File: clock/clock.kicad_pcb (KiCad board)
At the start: 2 copper layers, 100 x 50 mm, 51 parts, among them J1 Conn_01x16_Male, J2 Conn_01x16_Male, J3 5v, J4 Conn_01x01_Male, J5 24v, J6 Conn_01x01_Male, U1 iv12, U2 iv12, U3 iv12, U4 iv12, U5 ULN2003, U6 ULN2003, U7 ULN2003, U8 ULN2003

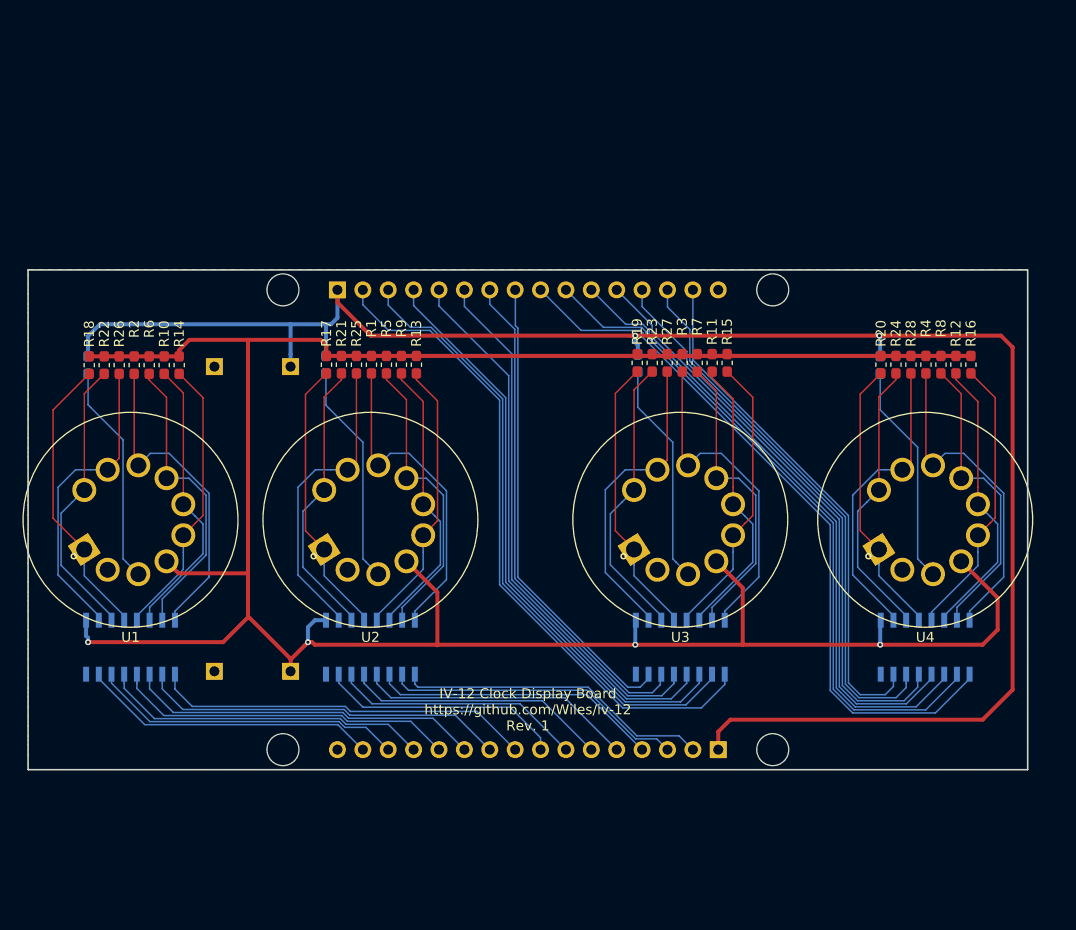
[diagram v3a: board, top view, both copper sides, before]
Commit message: Clock rev 2 with controller
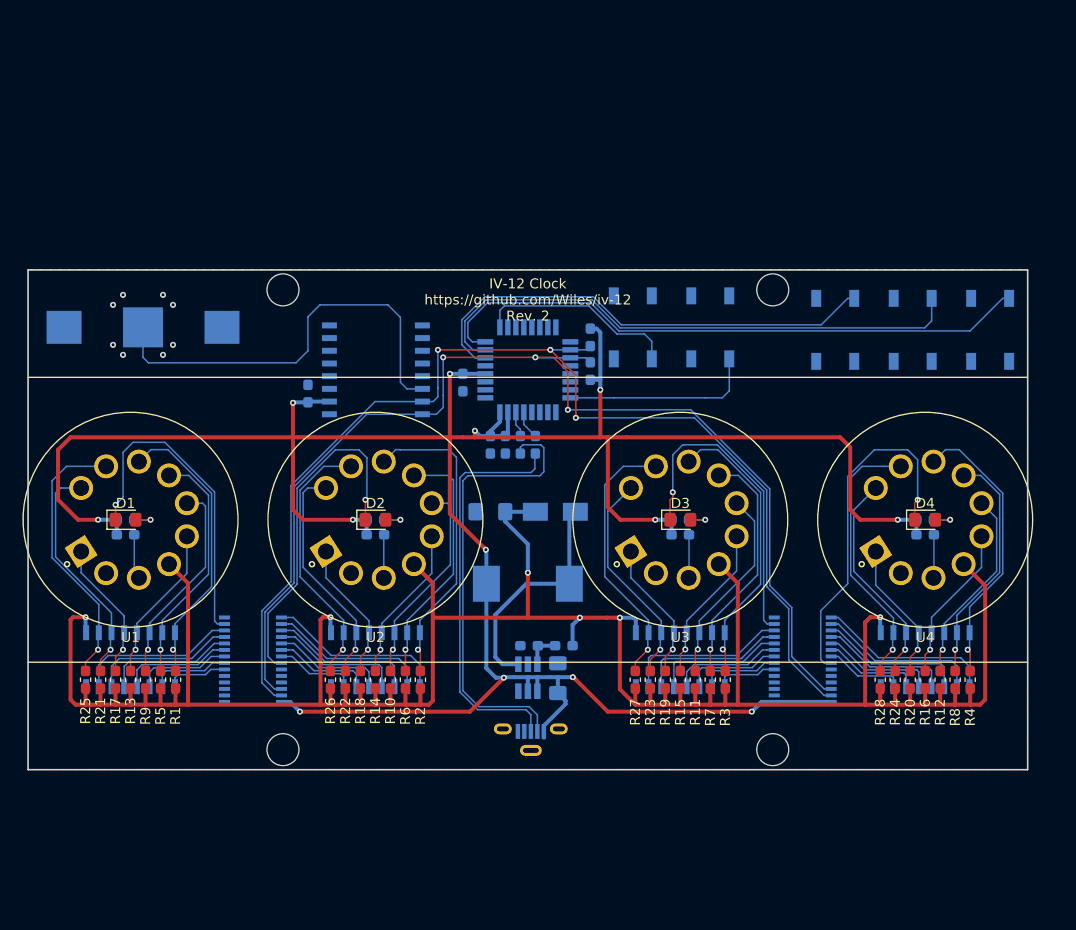
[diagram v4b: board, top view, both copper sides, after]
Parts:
- removed J2: Conn_01x16_Male, Connector_PinHeader_2.54mm:PinHeader_1x16_P2.54mm_Vertical
- removed J3: 5v, Connector_PinHeader_2.54mm:PinHeader_1x01_P2.54mm_Vertical
- removed J4, J6: Conn_01x01_Male, Connector_PinHeader_2.54mm:PinHeader_1x01_P2.54mm_Vertical
- removed J5: 24v, Connector_PinHeader_2.54mm:PinHeader_1x01_P2.54mm_Vertical
- removed the REF** at (127.0, 127.0)
- removed the REF** at (102.5, 150.0)
- removed the REF** at (151.5, 150.0)
- removed the REF** at (102.5, 104.0)
- removed the REF** at (151.5, 104.0)
- added BT1: 3v, Battery:BatteryHolder_Keystone_3000_1x12mm, B.Cu at (88.5, 107.8)
- added C1: 10u, Capacitor_SMD:C_1206_3216Metric_Pad1.42x1.75mm_HandSolder, B.Cu at (130.0, 142.8)
- added C2: 10u, Capacitor_SMD:C_1206_3216Metric_Pad1.42x1.75mm_HandSolder, B.Cu at (123.2, 126.2)
- added C3: .1u, Capacitor_SMD:C_0603_1608Metric_Pad1.05x0.95mm_HandSolder, B.Cu at (123.2, 119.5)
- added C4: .1u, Capacitor_SMD:C_0603_1608Metric_Pad1.05x0.95mm_HandSolder, B.Cu at (120.5, 113.3)
- added C5: .1u, Capacitor_SMD:C_0603_1608Metric_Pad1.05x0.95mm_HandSolder, B.Cu at (105.0, 114.4)
- added C6: .1u, Capacitor_SMD:C_0603_1608Metric_Pad1.05x0.95mm_HandSolder, B.Cu at (124.8, 119.5)
- added D1: LED_Small, LED_SMD:LED_0805_2012Metric_Pad1.15x1.40mm_HandSolder, F.Cu at (86.8, 127.0)
- added D2: LED_Small, LED_SMD:LED_0805_2012Metric_Pad1.15x1.40mm_HandSolder, F.Cu at (111.8, 127.0)
- added D3: LED_Small, LED_SMD:LED_0805_2012Metric_Pad1.15x1.40mm_HandSolder, F.Cu at (142.2, 127.0)
- added D4: LED_Small, LED_SMD:LED_0805_2012Metric_Pad1.15x1.40mm_HandSolder, F.Cu at (166.8, 127.0)
- added D5: D_Schottky, Diode_SMD:D_SMA, B.Cu at (129.8, 126.2)
- added L1: L_Small, Inductor_SMD:L_10.4x10.4_H4.8, B.Cu at (127.0, 133.4)
- added R33: 470, Resistor_SMD:R_0603_1608Metric_Pad1.05x0.95mm_HandSolder, B.Cu at (111.8, 127.0)
- added R34: 470, Resistor_SMD:R_0603_1608Metric_Pad1.05x0.95mm_HandSolder, B.Cu at (166.8, 127.0)
- added R35: 470, Resistor_SMD:R_0603_1608Metric_Pad1.05x0.95mm_HandSolder, B.Cu at (86.8, 127.0)
- added R36: 470, Resistor_SMD:R_0603_1608Metric_Pad1.05x0.95mm_HandSolder, B.Cu at (142.2, 127.0)
- added R37: 82k, Resistor_SMD:R_0603_1608Metric_Pad1.05x0.95mm_HandSolder, B.Cu at (130.6, 139.6)
- added R38: 2.2k, Resistor_SMD:R_0603_1608Metric_Pad1.05x0.95mm_HandSolder, B.Cu at (127.1, 139.6)
- added R39: 10k, Resistor_SMD:R_0603_1608Metric_Pad1.05x0.95mm_HandSolder, B.Cu at (133.2, 108.8)
- added R40: 10k, Resistor_SMD:R_0603_1608Metric_Pad1.05x0.95mm_HandSolder, B.Cu at (133.2, 112.1)
- added R41: 22, Resistor_SMD:R_0603_1608Metric_Pad1.05x0.95mm_HandSolder, B.Cu at (127.8, 119.5)
- added R42: 22, Resistor_SMD:R_0603_1608Metric_Pad1.05x0.95mm_HandSolder, B.Cu at (126.2, 119.5)
- added REF**: MountingHole_3.2mm_M3_DIN965, MountingHole:MountingHole_3.2mm_M3_DIN965, F.Cu at (102.5, 150.0)
- added REF**: MountingHole_3.2mm_M3_DIN965, MountingHole:MountingHole_3.2mm_M3_DIN965, F.Cu at (151.5, 150.0)
- added REF**: MountingHole_3.2mm_M3_DIN965, MountingHole:MountingHole_3.2mm_M3_DIN965, F.Cu at (102.5, 104.0)
- added REF**: MountingHole_3.2mm_M3_DIN965, MountingHole:MountingHole_3.2mm_M3_DIN965, F.Cu at (151.5, 104.0)
- added SW1: SW_SPST, Button_Switch_SMD:SW_SPST_TL3342, B.Cu at (165.5, 108.0)
- added SW2: SW_SPST, Button_Switch_SMD:SW_SPST_TL3342, B.Cu at (157.8, 108.0)
- added SW3: SW_SPST, Button_Switch_SMD:SW_SPST_TL3342, B.Cu at (145.2, 107.8)
- added SW4: SW_SPST, Button_Switch_SMD:SW_SPST_TL3342, B.Cu at (173.2, 108.0)
- added SW5: SW_SPST, Button_Switch_SMD:SW_SPST_TL3342, B.Cu at (137.5, 107.8)
- added U10: PCA9685PW, Package_SO:TSSOP-28_4.4x9.7mm_P0.65mm, B.Cu at (154.5, 141.0)
- added U11: ATmega32U2-AU, Package_QFP:TQFP-32_7x7mm_P0.8mm, B.Cu at (127.0, 112.0)
- added U12: DS3231M, Package_SO:SOIC-16W_7.5x10.3mm_P1.27mm, B.Cu at (111.8, 112.0)
- added U13: MT3608, Package_TO_SOT_SMD:SOT-23-6_Handsoldering, B.Cu at (127.0, 142.8)
- added U9: PCA9685PW, Package_SO:TSSOP-28_4.4x9.7mm_P0.65mm, B.Cu at (99.5, 141.0)
- J1: value Conn_01x16_Male -> USB_OTG-conn1; footprint Connector_PinHeader_2.54mm:PinHeader_1x16_P2.54mm_Vertical -> Connector_USB:USB_Micro-B_Molex-105133-0001
- moved R13 42.6 mm to (87.2, 143.0), turned to 90 degrees
- moved R2 42.5 mm to (116.2, 143.0), turned to 90 degrees
- moved R25 41.6 mm to (82.8, 143.0), turned to 90 degrees
- moved R18 41.6 mm to (110.2, 143.0), turned to 90 degrees
- moved R9 40.6 mm to (88.8, 143.0), turned to 90 degrees
- moved R6 40.6 mm to (114.8, 143.0), turned to 90 degrees
- moved R21 39.7 mm to (84.2, 143.0), turned to 90 degrees
- moved R22 39.7 mm to (108.8, 143.0), turned to 90 degrees
- moved R5 38.8 mm to (90.2, 143.0), turned to 90 degrees
- moved R10 38.8 mm to (113.2, 143.0), turned to 90 degrees
- moved R17 37.9 mm to (85.8, 143.0), turned to 90 degrees
- moved R26 37.9 mm to (107.2, 143.0), turned to 90 degrees
- moved R1 37.1 mm to (91.8, 143.0), turned to 90 degrees
- moved R14 37.1 mm to (111.8, 143.0), turned to 90 degrees
- moved R31 33.4 mm to (111.8, 128.5), turned to 180 degrees
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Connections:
- J1 pad 4: Net-(J1-Pad4) -> GND
- J1 pad 5: Net-(J1-Pad5) -> GND
- J1 pad 6: Net-(J1-Pad6) -> GND
- U1 pad 1: Net-(R18-Pad2) -> Net-(R17-Pad2)
- U1 pad 10: Net-(R22-Pad2) -> Net-(R21-Pad2)
- U1 pad 3: Net-(R31-Pad1) -> Net-(R30-Pad1)
- U1 pad 5: Net-(R14-Pad2) -> Net-(R13-Pad2)
- U1 pad 6: Net-(R10-Pad2) -> Net-(R9-Pad2)
- U1 pad 7: Net-(R6-Pad2) -> Net-(R5-Pad2)
- U1 pad 8: Net-(R2-Pad2) -> Net-(R1-Pad2)
- U1 pad 9: Net-(R26-Pad2) -> Net-(R25-Pad2)
- U2 pad 1: Net-(R17-Pad2) -> Net-(R18-Pad2)
- U2 pad 10: Net-(R21-Pad2) -> Net-(R22-Pad2)
- U2 pad 3: Net-(R30-Pad1) -> Net-(R31-Pad1)
- U2 pad 5: Net-(R13-Pad2) -> Net-(R14-Pad2)
- U2 pad 6: Net-(R9-Pad2) -> Net-(R10-Pad2)
- U2 pad 7: Net-(R5-Pad2) -> Net-(R6-Pad2)
- U2 pad 8: Net-(R1-Pad2) -> Net-(R2-Pad2)
- U2 pad 9: Net-(R25-Pad2) -> Net-(R26-Pad2)
- U5 pad 1: Net-(J1-Pad9) -> Net-(U5-Pad1)
- U5 pad 10: Net-(R26-Pad2) -> Net-(R25-Pad2)
- U5 pad 11: Net-(R22-Pad2) -> Net-(R21-Pad2)
- U5 pad 12: Net-(R18-Pad2) -> Net-(R17-Pad2)
- U5 pad 13: Net-(R14-Pad2) -> Net-(R13-Pad2)
- U5 pad 14: Net-(R10-Pad2) -> Net-(R9-Pad2)
- U5 pad 15: Net-(R6-Pad2) -> Net-(R5-Pad2)
- U5 pad 16: Net-(R2-Pad2) -> Net-(R1-Pad2)
- U5 pad 2: Net-(J1-Pad10) -> Net-(U5-Pad2)
- U5 pad 3: Net-(J1-Pad11) -> Net-(U5-Pad3)
- U5 pad 4: Net-(J1-Pad12) -> Net-(U5-Pad4)
- U5 pad 5: Net-(J1-Pad13) -> Net-(U5-Pad5)
- U5 pad 6: Net-(J1-Pad14) -> Net-(U5-Pad6)
- U5 pad 7: Net-(J1-Pad15) -> Net-(U5-Pad7)
- U6 pad 1: Net-(J1-Pad2) -> Net-(U6-Pad1)
- U6 pad 10: Net-(R25-Pad2) -> Net-(R26-Pad2)
- U6 pad 11: Net-(R21-Pad2) -> Net-(R22-Pad2)
- U6 pad 12: Net-(R17-Pad2) -> Net-(R18-Pad2)
- U6 pad 13: Net-(R13-Pad2) -> Net-(R14-Pad2)
- U6 pad 14: Net-(R9-Pad2) -> Net-(R10-Pad2)
- U6 pad 15: Net-(R5-Pad2) -> Net-(R6-Pad2)
- U6 pad 16: Net-(R1-Pad2) -> Net-(R2-Pad2)
- U6 pad 2: Net-(J1-Pad3) -> Net-(U6-Pad2)
- U6 pad 3: Net-(J1-Pad4) -> Net-(U6-Pad3)
- U6 pad 4: Net-(J1-Pad5) -> Net-(U6-Pad4)
- U6 pad 5: Net-(J1-Pad6) -> Net-(U6-Pad5)
- U6 pad 6: Net-(J1-Pad7) -> Net-(U6-Pad6)
- U6 pad 7: Net-(J1-Pad8) -> Net-(U6-Pad7)
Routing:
- net SDA: track 0.00 -> 115.5 mm, vias 0 -> 3
- net SCL: track 0.00 -> 114.8 mm, vias 0 -> 3
- net +5V: track 179.9 -> 274.7 mm, vias 2 -> 13
- net Net-(U10-Pad6): track 67.2 -> 6.25 mm
- net MODE: track 0.00 -> 60.9 mm
- net DOWN: track 0.00 -> 55.8 mm
- net Net-(U10-Pad7): track 62.8 -> 8.04 mm
- net Net-(U10-Pad15): track 72.3 -> 17.9 mm
- net Net-(U10-Pad16): track 68.2 -> 16.4 mm
- net Net-(U10-Pad17): track 64.2 -> 14.8 mm
- net Net-(U10-Pad8): track 59.1 -> 9.72 mm
- net UP: track 0.00 -> 47.9 mm
- net Net-(U10-Pad18): track 60.3 -> 12.6 mm
- net Net-(U10-Pad19): track 58.0 -> 11.4 mm
- net Net-(U10-Pad20): track 55.2 -> 9.69 mm
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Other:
- net class 24v removed
- net class 5v removed
- net class Power added: clearance 0.152, trace_width 0.4, via_dia 0.6, via_drill 0.3
- board text added: "IV-12 Clock https://github.com/Wiles/iv-12 Rev. 2"
- board text removed: "IV-12 Clock Display Board https://github.com/Wiles/iv-12 Rev. 1"
- board text removed: "MT3608"

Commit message: Rev 3 pcb
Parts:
- added C7: 22p, Capacitor_SMD:C_0603_1608Metric_Pad1.05x0.95mm_HandSolder, B.Cu at (123.7, 119.0)
- added C8: 22p, Capacitor_SMD:C_0603_1608Metric_Pad1.05x0.95mm_HandSolder, B.Cu at (130.8, 119.0)
- added C9: .1u, Capacitor_SMD:C_0603_1608Metric_Pad1.05x0.95mm_HandSolder, B.Cu at (124.5, 104.8)
- added R43: 10k, Resistor_SMD:R_0603_1608Metric_Pad1.05x0.95mm_HandSolder, B.Cu at (133.9, 119.0)
- added TP1: TestPoint, TestPoint:TestPoint_Plated_Hole_D2.0mm, F.Cu at (133.8, 149.1)
- added TP2: TestPoint, TestPoint:TestPoint_Plated_Hole_D2.0mm, F.Cu at (120.2, 149.2)
- added TP3: TestPoint, TestPoint:TestPoint_Plated_Hole_D2.0mm, F.Cu at (138.0, 149.2)
- added TP4: TestPoint, TestPoint:TestPoint_Plated_Hole_D2.0mm, F.Cu at (116.0, 149.2)
- added TP5: TestPoint, TestPoint:TestPoint_Plated_Hole_D2.0mm, F.Cu at (111.8, 149.2)
- added Y1: 16Mhz, Crystal:Crystal_SMD_5032-4Pin_5.0x3.2mm, B.Cu at (127.2, 119.0)
- U11: value ATmega32U2-AU -> ATmega32U4-AU; footprint Package_QFP:TQFP-32_7x7mm_P0.8mm -> Package_DFN_QFN:QFN-44-1EP_7x7mm_P0.5mm_EP5.15x5.15mm
- moved R41 24.2 mm to (119.5, 142.2)
- moved R42 23.3 mm to (121.0, 142.2)
- moved R39 16.2 mm to (120.7, 119.0)
- moved C3 16.0 mm to (129.5, 104.8), turned to 90 degrees
- moved R40 13.1 mm to (122.2, 119.0)
- moved SW3 7.75 mm to (137.5, 107.8)
- moved SW5 7.75 mm to (145.2, 107.8)
- moved C6 7.67 mm to (132.4, 119.0)
- moved U11 1.00 mm to (127.0, 111.0), turned to 180 degrees
- moved C4 0.37 mm to (120.8, 113.0), turned to 180 degrees
- moved J1 0.30 mm to (127.0, 149.0)
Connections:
- BT1 pad 1: GND -> Net-(BT1-Pad1)
- BT1 pad 2: Net-(BT1-Pad2) -> GND
- R39 pad 1: +5V -> SDA
- R39 pad 2: SDA -> +5V
- U11 pad 10: Net-(U11-Pad10) -> MODE
- U11 pad 11: Net-(U11-Pad11) -> OTHER
- U11 pad 13: Net-(U11-Pad13) -> RST
- U11 pad 14: Net-(U11-Pad14) -> +5V
- U11 pad 15: Net-(U11-Pad15) -> GND
- U11 pad 18: SDA -> SCL
- U11 pad 19: SCL -> SDA
- U11 pad 2: Net-(U11-Pad2) -> +5V
- U11 pad 23: Net-(U11-Pad23) -> GND
- U11 pad 24: RST -> +5V
- U11 pad 28: GND -> Net-(U11-Pad28)
- U11 pad 29: Net-(R41-Pad1) -> Net-(U11-Pad29)
- U11 pad 3: GND -> Net-(R42-Pad1)
- U11 pad 30: Net-(R42-Pad1) -> Net-(U11-Pad30)
- U11 pad 31: +5V -> Net-(U11-Pad31)
- U11 pad 32: +5V -> Net-(U11-Pad32)
- U11 pad 4: +5V -> Net-(R41-Pad1)
- U11 pad 5: Net-(U11-Pad5) -> GND
- U11 pad 6: UP -> Net-(U11-Pad6)
- U11 pad 7: DOWN -> Net-(U11-Pad7)
- U11 pad 8: MODE -> UP
- U11 pad 9: OTHER -> DOWN
- U12 pad 14: Net-(BT1-Pad2) -> Net-(BT1-Pad1)
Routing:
- net Net-(R42-Pad1): track 2.56 -> 64.3 mm, vias 0 -> 2
- net Net-(R41-Pad1): track 2.85 -> 62.6 mm, vias 0 -> 2
- net Net-(BT1-Pad2): track 42.9 -> 0.00 mm
- net Net-(J1-Pad2): track 45.2 -> 10.6 mm
- net Net-(J1-Pad3): track 40.6 -> 11.4 mm
- net Net-(BT1-Pad1): track 0.00 -> 28.3 mm
- net +5V: track 274.7 -> 301.5 mm
- net UP: track 47.9 -> 33.5 mm
- net DOWN: track 55.8 -> 41.5 mm
- net MODE: track 60.9 -> 48.1 mm
- net SCL: track 114.8 -> 123.6 mm
- net Net-(C8-Pad1): track 0.00 -> 8.70 mm
- net SDA: track 115.5 -> 122.9 mm, vias 3 -> 2
- net Net-(C7-Pad1): track 0.00 -> 6.70 mm
- net +24V: track 258.3 -> 264.7 mm, vias 6 -> 7
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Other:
- net class Power: trace_width 0.4 -> 0.25
- board text added: "IV-12 Clock https://github.com/Wiles/iv-12 Rev. 3"
- board text removed: "IV-12 Clock https://github.com/Wiles/iv-12 Rev. 2"
